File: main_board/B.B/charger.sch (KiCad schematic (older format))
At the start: 8 parts, among them U72 SE9017

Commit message: presuny_konektoru
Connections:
- net BAT: now also C76.1, U72.3 (VBAT); no longer C77.1, LED4.2 (A), LED5.2 (A), U72.4 (VCC)
- net VCC: now also C77.1, LED4.2 (A), LED5.2 (A), U72.4 (VCC); no longer C76.1, U72.3 (VBAT)
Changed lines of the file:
@@
 $Descr A4 11693 8268
 encoding utf-8
-Sheet 6 9
+Sheet 5 9
 Title ""
 Date ""
@@
 Wire Wire Line
 	6675 3400 6775 3400
+Text HLabel 6775 3400 2    50   Input ~ 0
+BAT
 Text HLabel 3900 3400 0    50   Input ~ 0
-BAT
-Text HLabel 6775 3400 2    50   Input ~ 0
 VCC
 $EndSCHEMATC

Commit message: new schema
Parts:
- removed C76, C77: 1uf, Resistor_SMD:R_0402_1005Metric, symbol B.B-rescue:C-Device-B.B-rescue
- removed LED4: RED, LED_SMD:LED_0603_1608Metric, symbol B.B-rescue:LED-B.B-eagle-import
- removed R16: 1k, Resistor_SMD:R_0402_1005Metric, symbol B.B-rescue:R-Device-B.B-rescue
- removed R48: 1.5k, Resistor_SMD:R_0603_1608Metric, symbol B.B-rescue:R-Device-B.B-rescue
- removed U72: SE9017, Package_TO_SOT_SMD:SOT-23-6, symbol B.B-rescue:SE9017-B.B-rescue
- added C? (x4): 22uf, Capacitor_SMD:C_0805_2012Metric, symbol B.B-rescue:C-Device-B.B-rescue
- added C? (x2): 10uf, Capacitor_SMD:C_0805_2012Metric, symbol B.B-rescue:C-Device-B.B-rescue
- added C? (x3): 0.1uf, Capacitor_SMD:C_0805_2012Metric, symbol B.B-rescue:C-Device-B.B-rescue
- added D?: D_Schottky, symbol Device:D_Schottky
- added L?: 22u, symbol Device:L
- added R?: 75m, Resistor_SMD:R_1206_3216Metric, symbol Device:R
- added U?: TP5100, symbol B.B-rescue:TP5100
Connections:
- net labels added: NC
- wire segments 17 -> 38
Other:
- moved on the sheet: LED5, R19

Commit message: spinana nabijecka a FT232 pcb
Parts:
- removed D?: D_Schottky, symbol Device:D_Schottky
- added D2: SS54, BB:DO-214AC, symbol B.B-rescue:D_Schottky-Device-B.B-rescue
- L1: renamed from L?; footprint (none) -> BB:SL00630H
- U64: renamed from U?; footprint (none) -> Package_DFN_QFN:QFN-16-1EP_4x4mm_P0.65mm_EP2.5x2.5mm_ThermalVias; LCSC (none) -> C379389
- gave numbers to parts that had none: 10

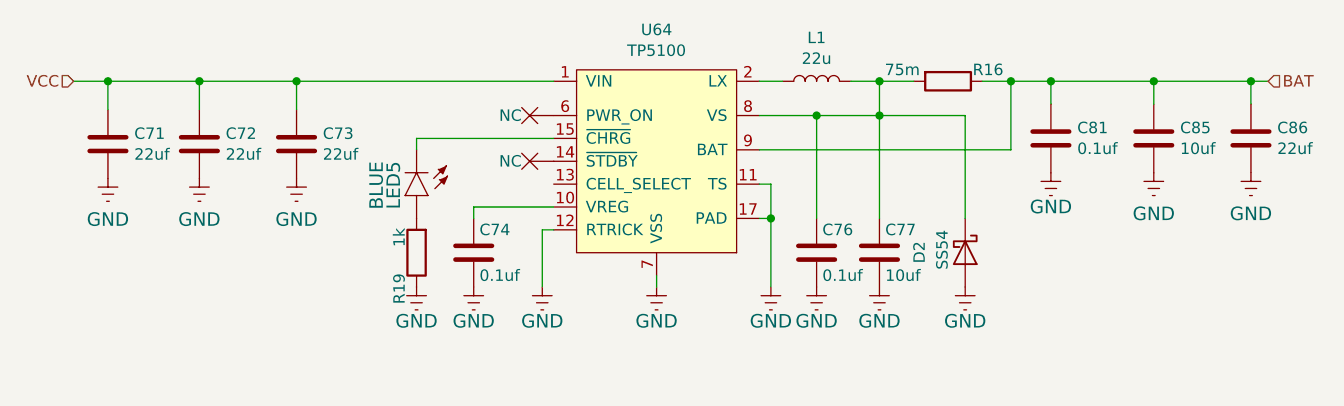
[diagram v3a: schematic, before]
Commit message: vymena rezistoru pro snimani nabijeciho proudu
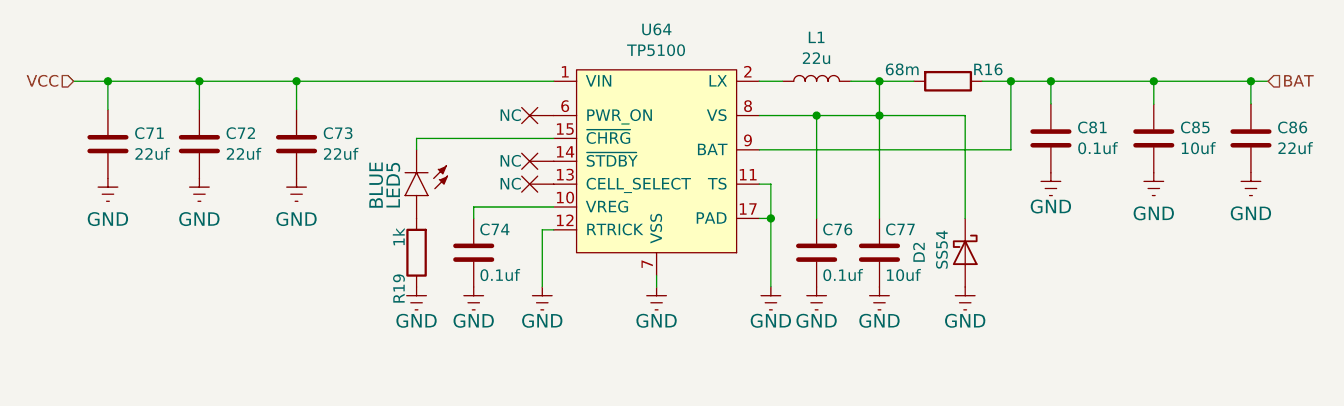
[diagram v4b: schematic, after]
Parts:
- L1: footprint BB:SL00630H -> BB:MCF-1040; LCSC C207843 -> C169268
- R16: value 75m -> 68m; footprint Resistor_SMD:R_1206_3216Metric -> Resistor_SMD:R_1210_3225Metric; LCSC C57963 -> C422195
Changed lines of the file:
@@
 F 0 "L1" V 6715 3125 50  0000 C CNN
 F 1 "22u" V 6624 3125 50  0000 C CNN
-F 2 "BB:SL00630H" H 6525 3125 50  0001 C CNN
+F 2 "BB:MCF-1040" H 6525 3125 50  0001 C CNN
 F 3 "~" H 6525 3125 50  0001 C CNN
-F 4 "C207843" V 6525 3125 50  0001 C CNN "LCSC"
+F 4 "C169268" V 6525 3125 50  0001 C CNN "LCSC"
 	1    6525 3125
 	0    -1   -1   0
@@
 P 7100 3125
 F 0 "R16" V 7050 3300 50  0000 C CNN
-F 1 "75m" V 7050 2925 50  0000 C CNN
-F 2 "Resistor_SMD:R_1206_3216Metric" V 7030 3125 50  0001 C CNN
+F 1 "68m" V 7050 2925 50  0000 C CNN
+F 2 "Resistor_SMD:R_1210_3225Metric" V 7030 3125 50  0001 C CNN
 F 3 "~" H 7100 3125 50  0001 C CNN
-F 4 "C57963" V 7100 3125 50  0001 C CNN "LCSC"
+F 4 "C422195" V 7100 3125 50  0001 C CNN "LCSC"
 	1    7100 3125
 	0    1    1    0
@@
 	0    1    1    0
 $EndComp
+$Comp
+L B.B-rescue:NC-B.B-eagle-import #NC?
+U 1 1 60B4EC06
+P 5375 3575
+AR Path="/5F77B818/60B4EC06" Ref="#NC?"  Part="1"
+AR Path="/5FB8FF0F/60B4EC06" Ref="#NC12"  Part="1"
+F 0 "#NC12" H 5375 3575 50  0001 C CNN
+F 1 "NC" H 5375 3575 50  0001 C CNN
+F 2 "" H 5375 3575 50  0001 C CNN
+F 3 "" H 5375 3575 50  0001 C CNN
+	1    5375 3575
+	-1   0    0    1
+$EndComp
 $EndSCHEMATC
